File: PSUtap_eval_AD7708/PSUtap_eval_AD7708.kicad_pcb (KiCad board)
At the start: 2 copper layers, 63.5 x 47 mm, 29 parts, among them J1 Analog_Inputs, J2 Conn_01x02, J3 Conn_01x10_Female, SW1 SW_Push, U1 AD7708-Analog_ADC-PSUtap_anal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, U2 AD780ANZ, Y1 Device_Crystal_Small

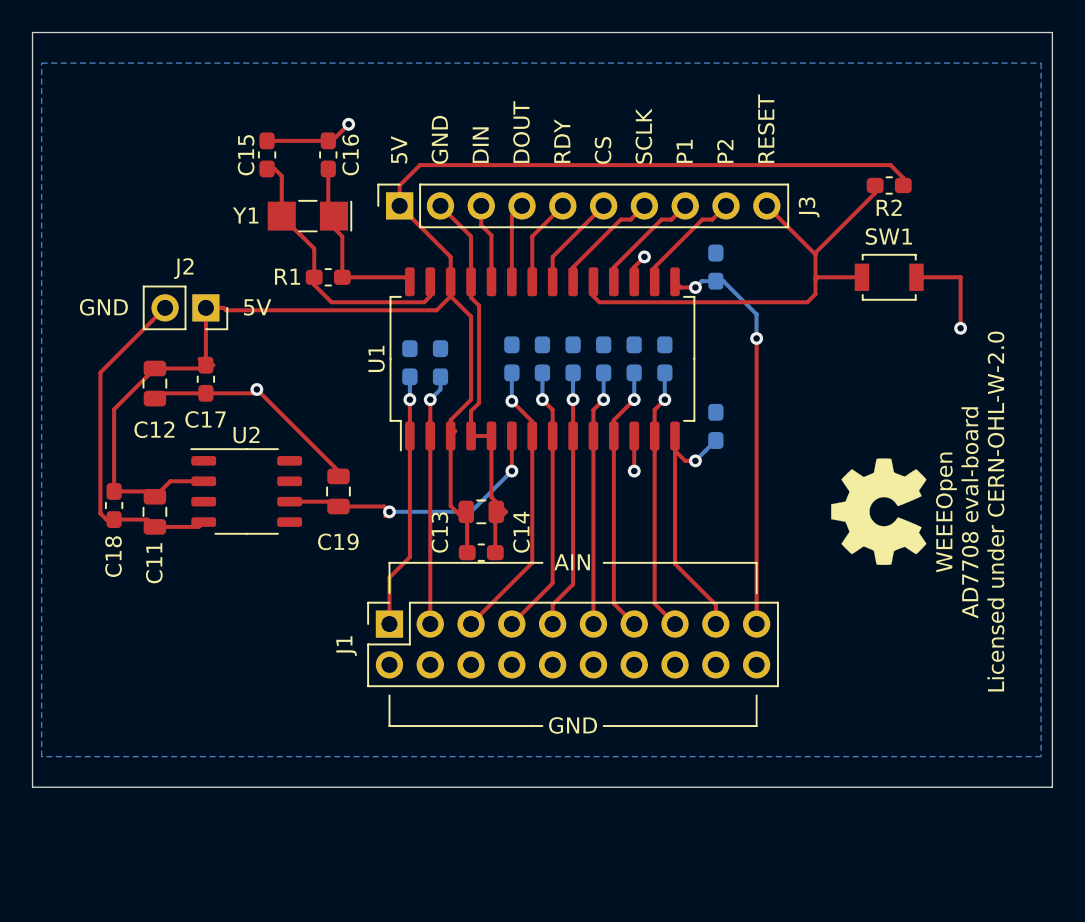
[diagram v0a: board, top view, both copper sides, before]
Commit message: single-sided evaluation board for AD7708
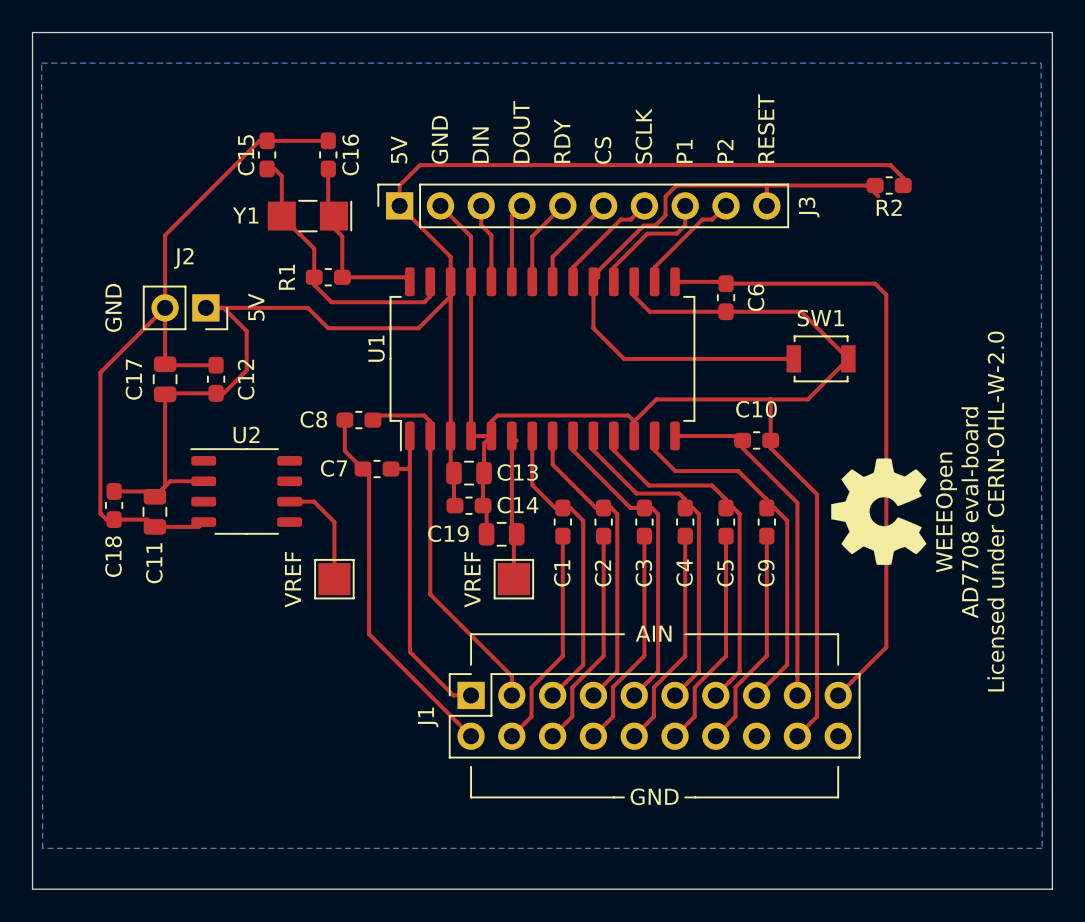
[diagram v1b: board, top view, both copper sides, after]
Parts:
- added VREF: TestPoint_Pad_2.0x2.0mm, TestPoint:TestPoint_Pad_2.0x2.0mm, F.Cu at (141.7, 110.2)
- added VREF: TestPoint_Pad_2.0x2.0mm, TestPoint:TestPoint_Pad_2.0x2.0mm, F.Cu at (130.6, 110.2)
- C1, C10, C2, C3, C4, C5, C6, C7, C8, C9: moved to F.Cu
- moved C9 12.0 mm to (157.5, 106.7), turned to 270 degrees
- moved C5 11.7 mm to (154.9, 106.7), turned to 270 degrees
- moved C4 11.4 mm to (152.4, 106.7), turned to 270 degrees
- moved C3 11.1 mm to (149.9, 106.7), turned to 270 degrees
- moved C2 10.9 mm to (147.3, 106.7), turned to 270 degrees
- moved C1 10.6 mm to (144.8, 106.7), turned to 270 degrees
- moved C19 10.5 mm to (141.0, 107.4), turned to 180 degrees
- moved C7 6.93 mm to (133.2, 103.4), turned to 180 degrees
- moved J1 6.75 mm to (139.1, 117.5)
- moved SW1 6.62 mm to (160.9, 96.5)
- moved C8 6.21 mm to (132.1, 100.3), turned to 180 degrees
- moved C14 3.02 mm to (138.9, 105.7)
- moved C10 2.69 mm to (156.8, 101.6), turned to 0 degrees
- moved C13 2.53 mm to (138.9, 103.6)
- moved C6 2.01 mm to (154.9, 92.7), turned to 270 degrees
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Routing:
- net GND: track 76.2 -> 238.4 mm, vias 5 -> 0
- net /A6: track 25.5 -> 39.7 mm, vias 2 -> 0
- net Net-(J3-Pad10): track 30.6 -> 39.1 mm
- net /A8: track 16.6 -> 23.0 mm, vias 1 -> 0
- net /A9: track 17.3 -> 22.9 mm, vias 1 -> 0
- net /A10: track 16.1 -> 21.6 mm, vias 1 -> 0
- net /A4: track 15.9 -> 21.3 mm, vias 1 -> 0
- net /A5: track 17.6 -> 22.6 mm, vias 1 -> 0
- net /A7: track 15.9 -> 19.6 mm, vias 1 -> 0
- net /A3: track 16.2 -> 19.7 mm, vias 1 -> 0
- net /A2: track 17.0 -> 19.9 mm, vias 1 -> 0
- net +5V: track 97.8 -> 96.1 mm
- net /VREF: track 17.7 -> 16.4 mm, vias 2 -> 0
- net /P1: track 6.93 -> 7.63 mm
- net /A1: track 18.6 -> 18.8 mm, vias 1 -> 0
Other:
- board size 63.5 x 47 mm -> 63.5 x 53.3 mm

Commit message: Shrink AD7708 PCB
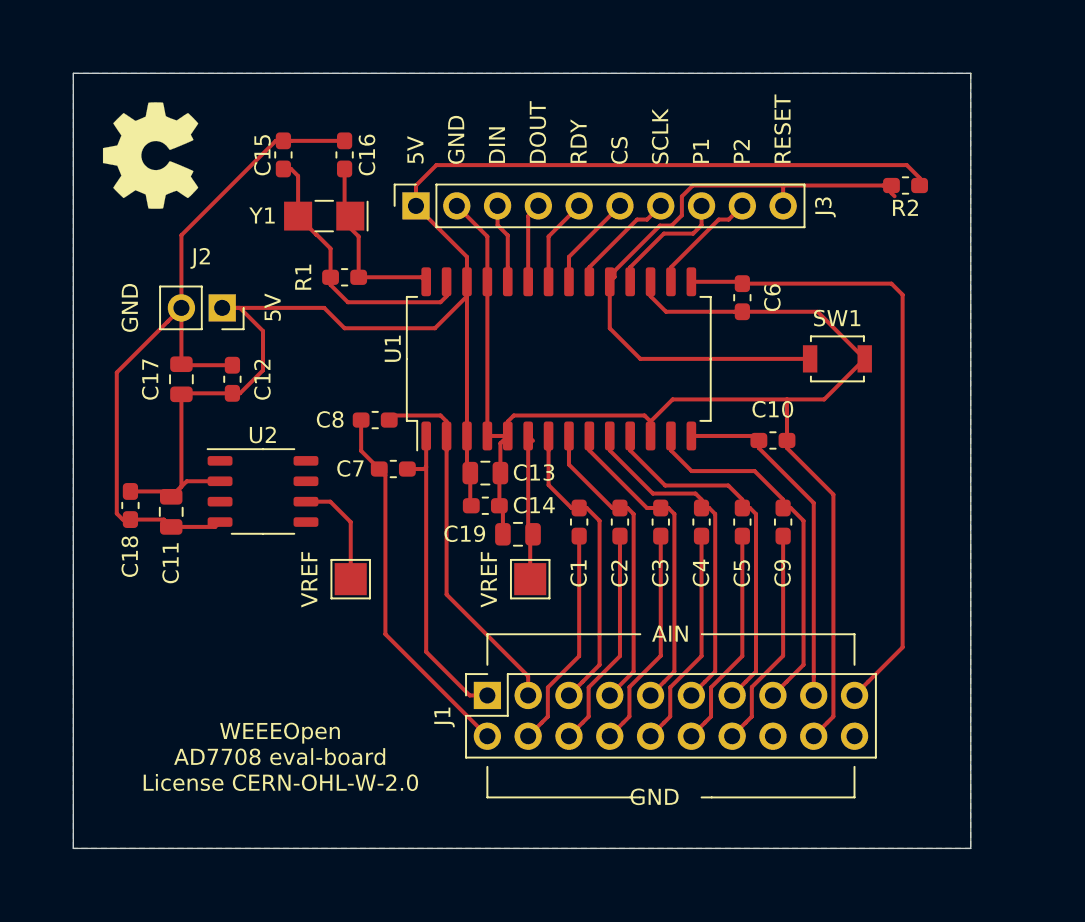
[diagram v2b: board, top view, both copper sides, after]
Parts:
- moved REF** 50.5 mm to (119.1, 83.9)
- moved C13 1.02 mm to (140.0, 103.6)
- moved C14 1.02 mm to (140.0, 105.7)
- moved C2 1.02 mm to (148.3, 106.7)
- moved C9 1.02 mm to (158.5, 106.7)
- moved R2 1.02 mm to (166.1, 85.7)
- moved U1 1.02 mm to (144.5, 96.5)
- moved C11 1.02 mm to (120.4, 106.0)
- moved C12 1.02 mm to (124.2, 97.8)
- moved C15 1.02 mm to (127.4, 83.8)
- moved C17 1.02 mm to (121.0, 97.8)
- moved U2 1.02 mm to (126.1, 104.8)
- moved C1 1.02 mm to (145.8, 106.7)
- moved C10 1.02 mm to (157.9, 101.6)
- moved C16 1.02 mm to (131.2, 83.8)
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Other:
- board size 63.5 x 53.3 mm -> 55.9 x 48.3 mm
- board text added: "WEEEOpen AD7708 eval-board License CERN-OHL-W-2.0"
- board text removed: "WEEEOpen AD7708 eval-board Licensed under CERN-OHL-W-2.0"

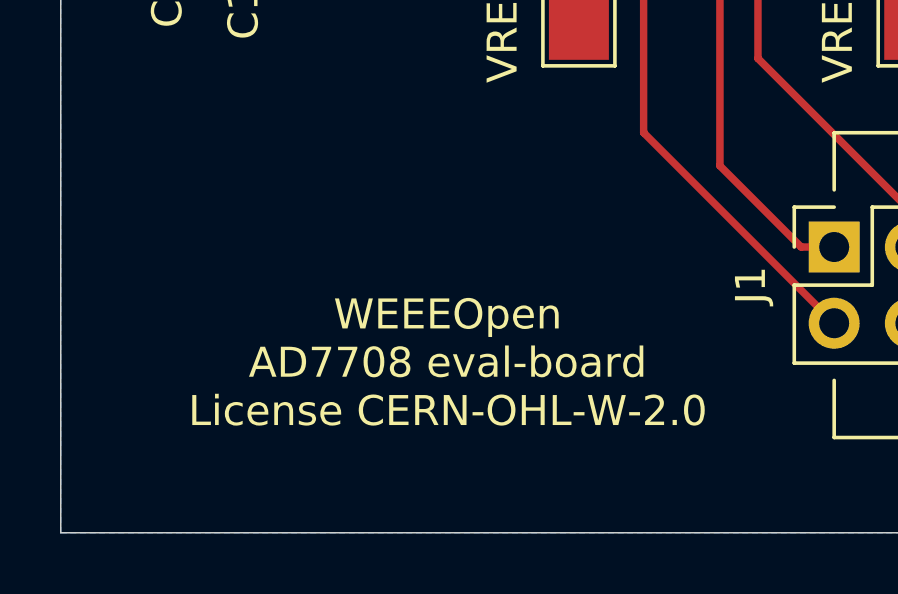
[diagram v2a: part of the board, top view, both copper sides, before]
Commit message: Separate WEEE and OPEN with space
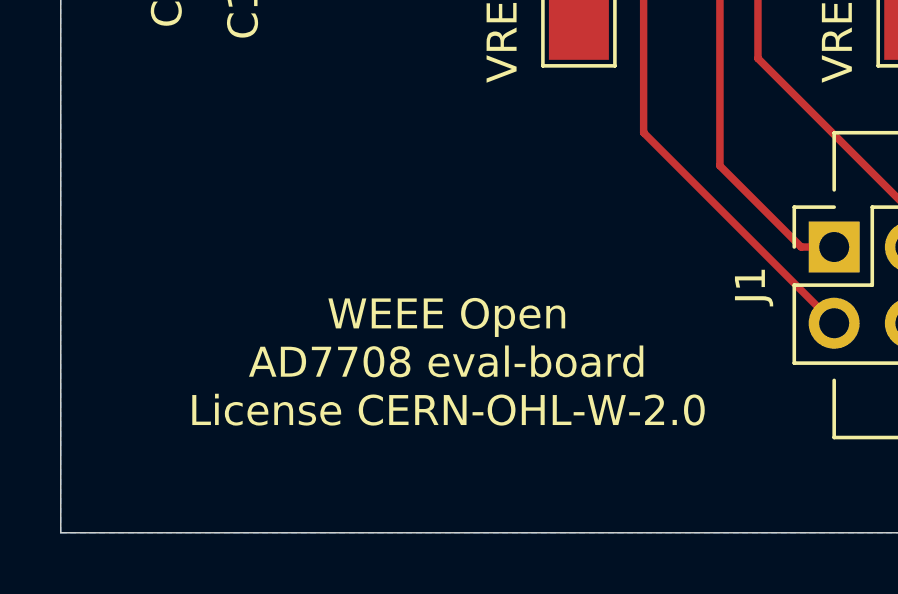
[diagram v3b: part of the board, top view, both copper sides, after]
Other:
- board text added: "WEEE Open AD7708 eval-board License CERN-OHL-W-2.0"
- board text removed: "WEEEOpen AD7708 eval-board License CERN-OHL-W-2.0"
